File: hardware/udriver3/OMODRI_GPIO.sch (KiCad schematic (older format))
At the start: 10 parts, among them U10 TPD4E001, U11 TPD4E001, U12 TPD4E001, U3 TMS320F28388D

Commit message: Power supply distribution updated.
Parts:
- C110: renamed from C113; footprint (none) -> Capacitor_SMD:C_0603_1608Metric; DigiKey (none) -> 490-10475-1-ND; Farnell (none) -> 2456110; Mouser (none) -> 81-GRM188R61A106ME9D; Part No (none) -> GRM188R61A106ME69D; RS (none) -> 113-8702; Rated Voltage (none) -> 10V
- C111: renamed from C114; footprint (none) -> Capacitor_SMD:C_0603_1608Metric; DigiKey (none) -> 490-10475-1-ND; Farnell (none) -> 2456110; Mouser (none) -> 81-GRM188R61A106ME9D; Part No (none) -> GRM188R61A106ME69D; RS (none) -> 113-8702; Rated Voltage (none) -> 10V
- renumbered C115 to C112, C116 to C113, R47 to R49, R48 to R50, U3 to U7
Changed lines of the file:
@@
 $EndDescr
 $Comp
-L omodri_lib:TMS320F28388D U3
+L omodri_lib:TMS320F28388D U7
 U 4 1 5F3A5B71
 P 1100 3050
-F 0 "U3" H 800 5150 60  0000 C CNN
+F 0 "U7" H 800 5150 60  0000 C CNN
 F 1 "TMS320F28388D" H 1100 5050 60  0000 C CNN
 F 2 "udriver3:F28388DZWTS" H 1100 5050 60  0001 C CNN
@@
 $EndComp
 $Comp
-L omodri_lib:TMS320F28388D U3
+L omodri_lib:TMS320F28388D U7
 U 5 1 5F3AD210
 P 2800 3050
-F 0 "U3" H 2500 5150 60  0000 C CNN
+F 0 "U7" H 2500 5150 60  0000 C CNN
 F 1 "TMS320F28388D" H 2800 5050 60  0000 C CNN
 F 2 "udriver3:F28388DZWTS" H 2800 5050 60  0001 C CNN
@@
 $EndComp
 $Comp
-L omodri_lib:TMS320F28388D U3
+L omodri_lib:TMS320F28388D U7
 U 6 1 5F3C0127
 P 4600 3050
-F 0 "U3" H 4300 5150 60  0000 C CNN
+F 0 "U7" H 4300 5150 60  0000 C CNN
 F 1 "TMS320F28388D" H 4600 5050 60  0000 C CNN
 F 2 "udriver3:F28388DZWTS" H 4600 5050 60  0001 C CNN
@@
 $EndComp
 $Comp
-L omodri_lib:TMS320F28388D U3
+L omodri_lib:TMS320F28388D U7
 U 7 1 5F3CEA6B
 P 6450 3050
-F 0 "U3" H 6150 5150 60  0000 C CNN
+F 0 "U7" H 6150 5150 60  0000 C CNN
 F 1 "TMS320F28388D" H 6450 5050 60  0000 C CNN
 F 2 "udriver3:F28388DZWTS" H 6450 5050 60  0001 C CNN
@@
 $EndComp
 $Comp
-L omodri_lib:TMS320F28388D U3
+L omodri_lib:TMS320F28388D U7
 U 8 1 5F3D4214
 P 8050 3050
-F 0 "U3" H 7750 5150 60  0000 C CNN
+F 0 "U7" H 7750 5150 60  0000 C CNN
 F 1 "TMS320F28388D" H 8050 5050 60  0000 C CNN
 F 2 "udriver3:F28388DZWTS" H 8050 5050 60  0001 C CNN
@@
 $EndComp
 $Comp
-L omodri_lib:TMS320F28388D U3
+L omodri_lib:TMS320F28388D U7
 U 9 1 5F3DE432
 P 9550 4750
-F 0 "U3" H 9250 6850 60  0000 C CNN
+F 0 "U7" H 9250 6850 60  0000 C CNN
 F 1 "TMS320F28388D" H 9550 6750 60  0000 C CNN
 F 2 "udriver3:F28388DZWTS" H 9550 6750 60  0001 C CNN
@@
 	1750 2250 1800 2250
 $Comp
-L omodri_lib:TMS320F28388D U3
+L omodri_lib:TMS320F28388D U7
 U 3 1 5F3B32A9
 P 3650 6650
-F 0 "U3" H 3250 8750 60  0000 C CNN
+F 0 "U7" H 3250 8750 60  0000 C CNN
 F 1 "TMS320F28388D" H 3550 8650 60  0000 C CNN
 F 2 "udriver3:F28388DZWTS" H 3650 8650 60  0001 C CNN
@@
 P 2200 4950
 AR Path="/5F3A3F16/601171AE" Ref="C?"  Part="1"
-AR Path="/5F3A5338/601171AE" Ref="C116"  Part="1"
-F 0 "C116" H 2315 4996 50  0000 L CNN
+AR Path="/5F3A5338/601171AE" Ref="C113"  Part="1"
+F 0 "C113" H 2315 4996 50  0000 L CNN
 F 1 "100nF" H 2315 4905 50  0000 L CNN
 F 2 "Capacitor_SMD:C_0201_0603Metric" H 2238 4800 50  0001 C CNN
@@
 P 1350 5350
 AR Path="/5F3A3F16/601171B8" Ref="C?"  Part="1"
-AR Path="/5F3A5338/601171B8" Ref="C114"  Part="1"
-F 0 "C114" H 1465 5396 50  0000 L CNN
+AR Path="/5F3A5338/601171B8" Ref="C111"  Part="1"
+F 0 "C111" H 1465 5396 50  0000 L CNN
 F 1 "10uF" H 1465 5305 50  0000 L CNN
-F 2 "" H 1388 5200 50  0001 C CNN
-F 3 "~" H 1350 5350 50  0001 C CNN
+F 2 "Capacitor_SMD:C_0603_1608Metric" H 1388 5200 50  0001 C CNN
+F 3 "https://www.murata.com/en-eu/products/productdetail?partno=GRM188R61A106ME69%23" H 1350 5350 50  0001 C CNN
+F 4 "490-10475-1-ND" H 1350 5350 50  0001 C CNN "DigiKey"
+F 5 "2456110" H 1350 5350 50  0001 C CNN "Farnell"
+F 6 "81-GRM188R61A106ME9D" H 1350 5350 50  0001 C CNN "Mouser"
+F 7 "GRM188R61A106ME69D" H 1350 5350 50  0001 C CNN "Part No"
+F 8 "113-8702" H 1350 5350 50  0001 C CNN "RS"
+F 9 "10V" H 1350 5350 50  0001 C CNN "Rated Voltage"
 	1    1350 5350
 	1    0    0    -1
@@
 P 1750 4950
 AR Path="/5F3A3F16/6012246A" Ref="C?"  Part="1"
-AR Path="/5F3A5338/6012246A" Ref="C115"  Part="1"
-F 0 "C115" H 1865 4996 50  0000 L CNN
+AR Path="/5F3A5338/6012246A" Ref="C112"  Part="1"
+F 0 "C112" H 1865 4996 50  0000 L CNN
 F 1 "100nF" H 1865 4905 50  0000 L CNN
 F 2 "Capacitor_SMD:C_0201_0603Metric" H 1788 4800 50  0001 C CNN
@@
 P 950 5350
 AR Path="/5F3A3F16/6012351A" Ref="C?"  Part="1"
-AR Path="/5F3A5338/6012351A" Ref="C113"  Part="1"
-F 0 "C113" H 1065 5396 50  0000 L CNN
+AR Path="/5F3A5338/6012351A" Ref="C110"  Part="1"
+F 0 "C110" H 1065 5396 50  0000 L CNN
 F 1 "10uF" H 1065 5305 50  0000 L CNN
-F 2 "" H 988 5200 50  0001 C CNN
-F 3 "~" H 950 5350 50  0001 C CNN
+F 2 "Capacitor_SMD:C_0603_1608Metric" H 988 5200 50  0001 C CNN
+F 3 "https://www.murata.com/en-eu/products/productdetail?partno=GRM188R61A106ME69%23" H 950 5350 50  0001 C CNN
+F 4 "490-10475-1-ND" H 950 5350 50  0001 C CNN "DigiKey"
+F 5 "2456110" H 950 5350 50  0001 C CNN "Farnell"
+F 6 "81-GRM188R61A106ME9D" H 950 5350 50  0001 C CNN "Mouser"
+F 7 "GRM188R61A106ME69D" H 950 5350 50  0001 C CNN "Part No"
+F 8 "113-8702" H 950 5350 50  0001 C CNN "RS"
+F 9 "10V" H 950 5350 50  0001 C CNN "Rated Voltage"
 	1    950  5350
 	1    0    0    -1
@@
 P 950 5550
 AR Path="/5F3A3F16/60134E20" Ref="#PWR?"  Part="1"
-AR Path="/5F3A5338/60134E20" Ref="#PWR089"  Part="1"
-F 0 "#PWR089" H 950 5300 50  0001 C CNN
+AR Path="/5F3A5338/60134E20" Ref="#PWR092"  Part="1"
+F 0 "#PWR092" H 950 5300 50  0001 C CNN
 F 1 "GND" H 955 5377 50  0000 C CNN
 F 2 "" H 950 5550 50  0001 C CNN
@@
 P 1350 5550
 AR Path="/5F3A3F16/60136691" Ref="#PWR?"  Part="1"
-AR Path="/5F3A5338/60136691" Ref="#PWR090"  Part="1"
-F 0 "#PWR090" H 1350 5300 50  0001 C CNN
+AR Path="/5F3A5338/60136691" Ref="#PWR093"  Part="1"
+F 0 "#PWR093" H 1350 5300 50  0001 C CNN
 F 1 "GND" H 1355 5377 50  0000 C CNN
 F 2 "" H 1350 5550 50  0001 C CNN
@@
 P 1750 5150
 AR Path="/5F3A3F16/60137F4A" Ref="#PWR?"  Part="1"
-AR Path="/5F3A5338/60137F4A" Ref="#PWR091"  Part="1"
-F 0 "#PWR091" H 1750 4900 50  0001 C CNN
+AR Path="/5F3A5338/60137F4A" Ref="#PWR094"  Part="1"
+F 0 "#PWR094" H 1750 4900 50  0001 C CNN
 F 1 "GND" H 1755 4977 50  0000 C CNN
 F 2 "" H 1750 5150 50  0001 C CNN
@@
 P 2200 5150
 AR Path="/5F3A3F16/60139951" Ref="#PWR?"  Part="1"
-AR Path="/5F3A5338/60139951" Ref="#PWR092"  Part="1"
-F 0 "#PWR092" H 2200 4900 50  0001 C CNN
+AR Path="/5F3A5338/60139951" Ref="#PWR095"  Part="1"
+F 0 "#PWR095" H 2200 4900 50  0001 C CNN
 F 1 "GND" H 2205 4977 50  0000 C CNN
 F 2 "" H 2200 5150 50  0001 C CNN
@@
 P 2650 6550
 AR Path="/5F3A3F16/60145C31" Ref="#PWR?"  Part="1"
-AR Path="/5F3A5338/60145C31" Ref="#PWR093"  Part="1"
-F 0 "#PWR093" H 2650 6300 50  0001 C CNN
+AR Path="/5F3A5338/60145C31" Ref="#PWR096"  Part="1"
+F 0 "#PWR096" H 2650 6300 50  0001 C CNN
 F 1 "GND" H 2655 6377 50  0000 C CNN
 F 2 "" H 2650 6550 50  0001 C CNN
@@
 	2650 6450 2900 6450
 $Comp
-L Device:R R47
+L Device:R R49
 U 1 1 601DCDD1
 P 950 5000
-F 0 "R47" H 1020 5046 50  0000 L CNN
+F 0 "R49" H 1020 5046 50  0000 L CNN
 F 1 "0.1" H 1020 4955 50  0000 L CNN
 F 2 "" V 880 5000 50  0001 C CNN
@@
 $EndComp
 $Comp
-L Device:R R48
+L Device:R R50
 U 1 1 601DD13D
 P 1350 5000
-F 0 "R48" H 1420 5046 50  0000 L CNN
+F 0 "R50" H 1420 5046 50  0000 L CNN
 F 1 "0.1" H 1420 4955 50  0000 L CNN
 F 2 "" V 1280 5000 50  0001 C CNN
@@
 P 5700 5250
 AR Path="/5F3A3F16/6021D4E9" Ref="#PWR?"  Part="1"
-AR Path="/5F3A5338/6021D4E9" Ref="#PWR094"  Part="1"
-F 0 "#PWR094" H 5700 5000 50  0001 C CNN
+AR Path="/5F3A5338/6021D4E9" Ref="#PWR097"  Part="1"
+F 0 "#PWR097" H 5700 5000 50  0001 C CNN
 F 1 "GND" H 5705 5077 50  0000 C CNN
 F 2 "" H 5700 5250 50  0001 C CNN
@@
 P 6900 6050
 AR Path="/5F3A3F16/60471146" Ref="#PWR?"  Part="1"
-AR Path="/5F3A5338/60471146" Ref="#PWR096"  Part="1"
-F 0 "#PWR096" H 6900 5800 50  0001 C CNN
+AR Path="/5F3A5338/60471146" Ref="#PWR099"  Part="1"
+F 0 "#PWR099" H 6900 5800 50  0001 C CNN
 F 1 "GND" H 6905 5877 50  0000 C CNN
 F 2 "" H 6900 6050 50  0001 C CNN
@@
 P 5800 7250
 AR Path="/5F3A3F16/60476AD7" Ref="#PWR?"  Part="1"
-AR Path="/5F3A5338/60476AD7" Ref="#PWR095"  Part="1"
-F 0 "#PWR095" H 5800 7000 50  0001 C CNN
+AR Path="/5F3A5338/60476AD7" Ref="#PWR098"  Part="1"
+F 0 "#PWR098" H 5800 7000 50  0001 C CNN
 F 1 "GND" H 5805 7077 50  0000 C CNN
 F 2 "" H 5800 7250 50  0001 C CNN

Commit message: Updated version with 28388D pin matching PAL design.
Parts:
- R73: renamed from R49; footprint (none) -> Resistor_SMD:R_0201_0603Metric; DigiKey (none) -> P.10AKCT-ND; Farnell (none) -> 2797520; Mouser (none) -> 667-ERJ-2BSFR10X; Part No (none) -> ERJ-2BSFR10X; RS (none) -> 812-6633
- R74: renamed from R50; footprint (none) -> Resistor_SMD:R_0201_0603Metric; DigiKey (none) -> P.10AKCT-ND; Farnell (none) -> 2797520; Mouser (none) -> 667-ERJ-2BSFR10X; Part No (none) -> ERJ-2BSFR10X; RS (none) -> 812-6633
- U4: renamed from U7; DigiKey (none) -> 296-F28388DZWTS-ND; Mouser (none) -> 595-F28388DZWTS; Part No (none) -> F28388DZWTS
- renumbered C110 to C134, C111 to C135, C112 to C136, C113 to C137, U10 to U12, U12 to U13
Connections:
- net labels added: CAN_RX, CAN_TX, FSI_RXA_CLK, FSI_RXA_D0, FSI_RXA_D1, FSI_RX_EN, FSI_TXA_CLK, FSI_TXA_D0, FSI_TXA_D1, FSI_TX_EN, REF_3V0_BUF, ~COM_SPI_CS~, ~DRV1_GPIO_CSn~, ~DRV1_GPIO_FAULTn~, ~DRV2_GPIO_CSn~, ~DRV2_GPIO_FAULTn~
- net labels removed: COM_SPI_CS, DRV1_GPIO_CS, DRV2_GPIO_CS, REF_3V0, ~DRV1_GPIO_nFAULT~, ~DRV2_GPIO_nFAULT~
- wire segments 94 -> 104
- no-connect marks 0 -> 139
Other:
- moved on the sheet: C134, C135, C136, C137, R73, R74, U4C, U4F, U4G, U4H, U4I

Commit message: All footprints are present. DRV with 2 power branches.
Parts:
- removed U11, U12, U13: TPD4E001, symbol omodri_lib:TPD4E001
- added U17, U18, U19, U20: TPD2E001, Package_SO:Texas_R-PDSO-N5, symbol omodri_lib:TPD2E001
- U4: footprint udriver3:F28388DZWTS -> udrive3:NFBGA_337
- renumbered C134 to C148, C135 to C149, C136 to C150, C137 to C151, R73 to R80, R74 to R81
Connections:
- net labels added: ANALOG_IN1, ANALOG_IN2, GPIO0, GPIO1, GPIO2, GPIO3, GPIO4, GPIO5, SPI_CLK, SPI_SIMO, SPI_SOMI, WS2812B_CMD, ~COM_SPI_CSn~, ~SPI_CSn~
- net labels removed: DEBUG_INT_PIN1, DEBUG_INT_PIN2, ~COM_SPI_CS~
- wire segments 104 -> 121
- no-connect marks 139 -> 126
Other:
- moved on the sheet: U4D

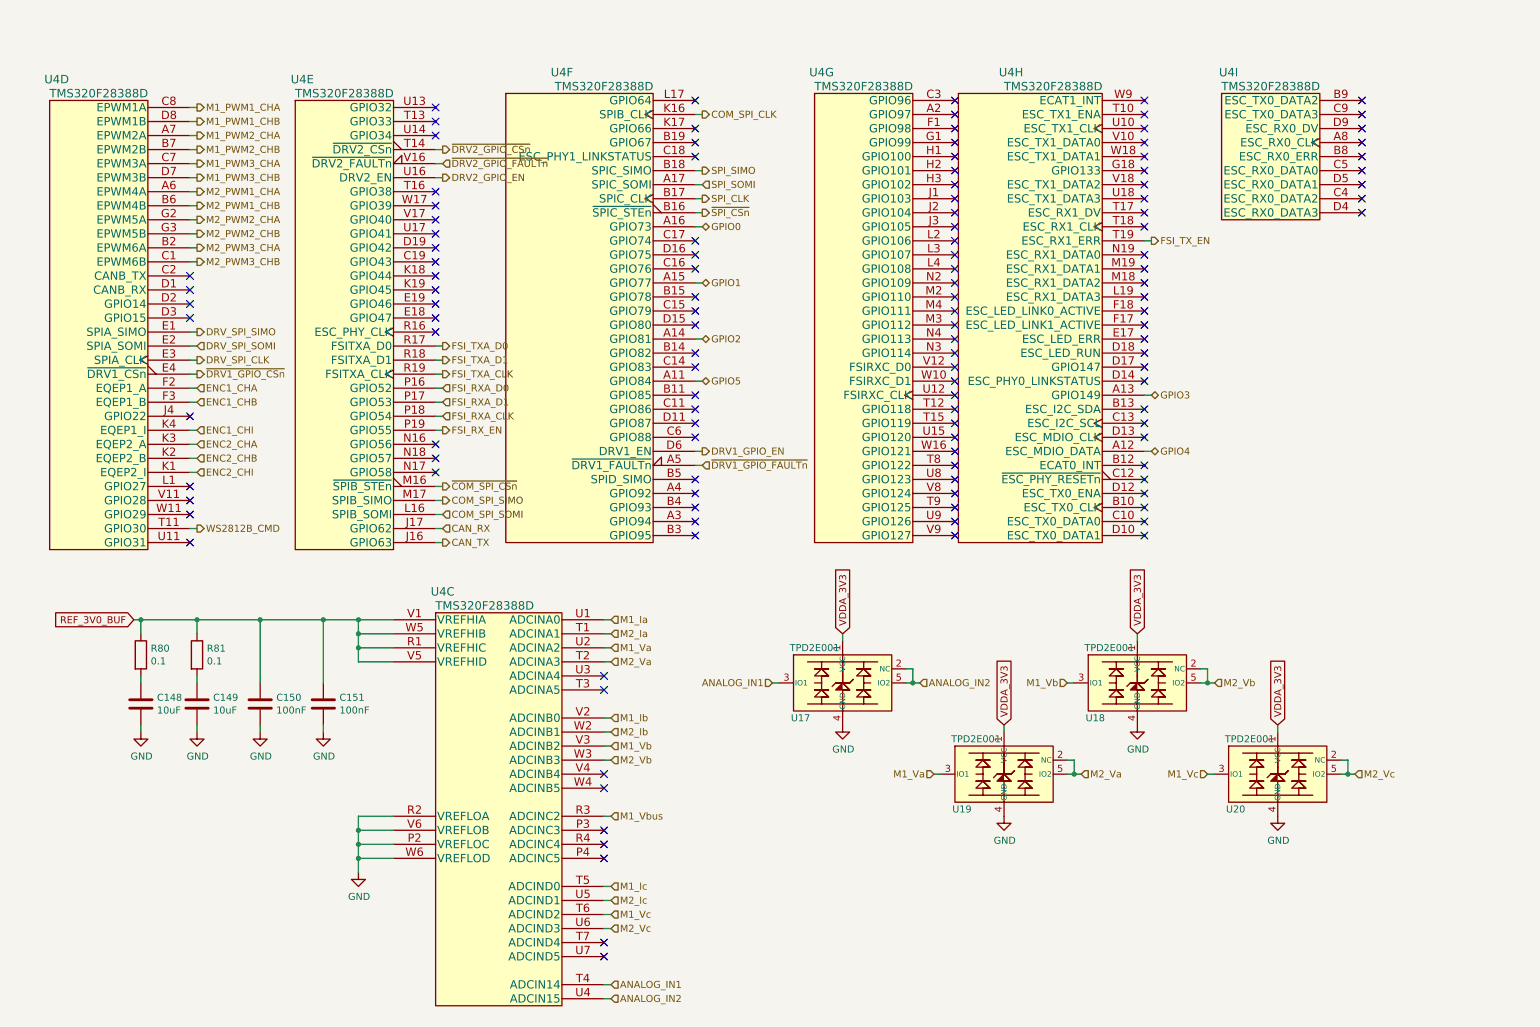
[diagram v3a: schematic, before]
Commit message: First complete release. No EtherCAT, IO ready to be connected.
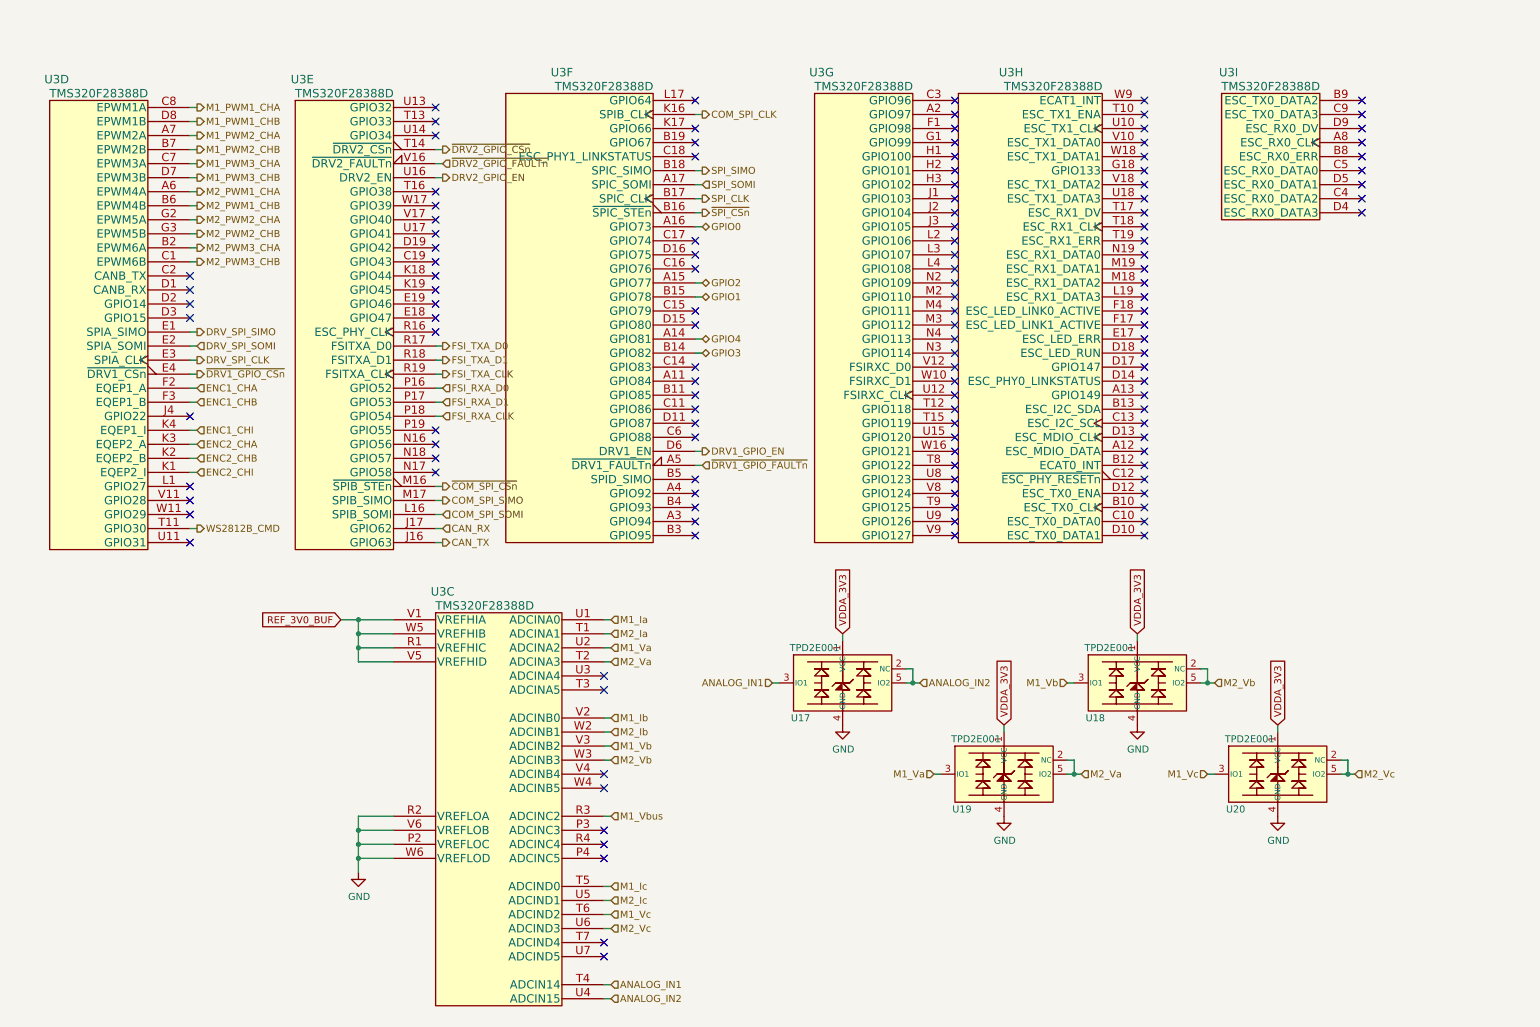
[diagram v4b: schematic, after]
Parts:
- removed C148, C149: 10uF, Capacitor_SMD:C_0603_1608Metric, symbol Device:C
- removed C150, C151: 100nF, Capacitor_SMD:C_0201_0603Metric, symbol Device:C
- removed R80, R81: 0.1, Resistor_SMD:R_0201_0603Metric, symbol Device:R
- renumbered U4 to U3
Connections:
- net GPIO1: now also U3.B15 (GPIO78); no longer U3.A15 (GPIO77)
- net GPIO2: now also U3.A15 (GPIO77); no longer U3.A14 (GPIO81)
- net GPIO3: now also U3.B14 (GPIO82); no longer U3.A13 (GPIO149)
- net GPIO4: now also U3.A14 (GPIO81); no longer U3.A12 (ESC_MDIO_DATA)
- net FSI_RX_EN: no longer names the net of U3.P19 (GPIO55)
- net FSI_TX_EN: no longer names the net of U3.T19 (ESC_RX1_ERR)
- net GPIO5: no longer names the net of U3.A11 (GPIO84)
- no-connect marks 126 -> 129
